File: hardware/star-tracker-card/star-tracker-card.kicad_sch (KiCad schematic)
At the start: 0 parts

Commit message: More EAGLE import cleanup
Fixed sheets, did some ERC cleanup, imported into layout, impmorted 4 layer DRC rules.
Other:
- company: (none) -> Portland State Aerospace Society
- title: (none) -> OreSat Star Tracker

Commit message: Schematic Overhaul of v1.3
Changed schematic to hierarchical, changed debug connector, updated OPD, removed JTAG, and ESD protection on removed connectors
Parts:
- added C42, C43: 22uF, oresat-passives:0805-B-NOSILK, symbol Device:C_Small
- added C45: 10u 25V 0805, Capacitor_SMD:C_1206_3216Metric, symbol Device:C
- added J1: ORESAT-DEBUG-CONNECTOR-CARD, oresat-connectors:J-JST-SM14BSHLSTF, symbol oresat-connectors:ORESAT-DEBUG-CONNECTOR-3
- added J101: 3-1734592-64-1734592-0, star-tracker-card:TE_3-1734592-6, symbol star-tracker-card-eagle-import:3-1734592-64-1734592-0
- added J4: TFM-120-01-L-D-RA, oresat-connectors:J-SAMTEC-TFM-120-X1-XXX-D-RA, symbol oresat-connectors:J-SAMTEC-TFM-120-01-L-D-RA
- added TP183, TP184, TP60, TP61, TP62: TEST-POINT3X4, oresat-misc:TestPoint_Pad_D1.0mm, symbol oresat-misc:Test-Point-1mm-round
- added TP32: Test-Point, oresat-misc:TestPoint_Pad_D1.0mm, symbol oresat-misc:Test-Point-1mm-round
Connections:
- new net: J1.8 (DEBUG-0), TP32.1
- new net: J4.1, J4.2, TP62.1
- new net: J4.5, J4.6, TP60.1
- new net: J4.3, J4.4, TP61.1
- new net: J4.32, J4.33, TP184.1
- new net: J4.34, J4.35, TP183.1
- new net 3.3V: C42.1, C43.1, J101.31, J101.32, J101.33
- new net C3-UART-RX: J4.38
- new net C3-UART-TX: J4.37
- new net CAN2_H: J4.17, J4.18
- new net CAN2_L: J4.19, J4.20
- new net CLK_EN_E: J101.23
- new net D0_E: J101.12
- new net D10_E: J101.16
- new net D11_E: J101.17
- new net D1_E: J101.11
- new net D2_E: J101.10
- new net D3_E: J101.9
- new net D4_E: J101.8
- new net D5_E: J101.7
- new net D6_E: J101.6
- new net D7_E: J101.13
- new net D8_E: J101.14
- new net D9_E: J101.15
- new net FLASH_E: J101.28
- new net GND: C42.2, C43.2, C45.2, J1.14 (GND), J1.15 (PAD), J1.16 (PAD), J1.5 (GND), J101.1, J101.18, J101.19, J101.2, J101.20, J101.34, J101.35, J101.36, J101.S1 (PAD), J101.S2 (PAD), J4.27, J4.28, J4.29, J4.30
- new net HSYNC_E: J101.4
- new net I2C2_SCL: J101.21
- new net I2C2_SDA: J101.22
- new net OPD_PWR: J4.15, J4.16
- new net OPD_SCL: J4.13, J4.14
- new net OPD_SDA: J4.11, J4.12
- new net PIXCLK_E: J101.5
- new net SADDR_E: J101.27
- new net STANDBY_E: J101.25
- new net TRIGGER_E: J101.29
- new net UART0_RX: J1.7 (CARD-RX)
- new net UART0_TX: J1.6 (CARD-TX)
- new net USB_CLI_N: J1.4 (DEVICE-D-)
- new net USB_CLI_P: J1.3 (DEVICE-D+)
- new net VBUS: C45.1, J4.23, J4.24, J4.25, J4.26
- new net VREG_EN_E: J101.30
- new net VSYNC_E: J101.3
- new net V_USB: J1.1 (VBUSP), J1.2 (VBUSP)
- new net ~{OE_E}: J101.26
- new net ~{RESET_E}: J101.24
- no-connect marks 0 -> 15
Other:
- sheet star-tracker-card_2 renamed Card Power Domain
- sheet star-tracker-card_3 renamed SIP C
- sheet star-tracker-card_4 renamed SIP B
- sheet star-tracker-card_5 renamed SIP A, E ,F
- removed sheet star-tracker-card_1
- added sheet Camera Logical Level Shifters (Level_Shifter.kicad_sch)
- added sheet SIP D (SIP_D.kicad_sch)
- sheet Card Power Domain ports: added C3-UART-RX, C3-UART-TX, OPD_PWR, OPD_SCL, OPD_SDA, SW_COM1, SW_COM2; removed none
- sheet SIP A, E ,F ports: added VIN_USB; removed none
- sheet SIP B ports: added USB_CLI_N, USB_CLI_P, USB_CLI_VBUS, VIN_USB; removed none
- sheet SIP C ports: added CAN2_H, CAN2_L, D0_I, D10_I, D11_I, D1_I, D2_I, D3_I, D4_I, D5_I, D6_I, D7_I, D8_I, D9_I, HSYNC_I, PIXCLK_I, SCL_2, SDA_2, UART0_RX, UART0_TX, VSYNCI; removed none
- note added: "36 Pin connector Camera Connector"
- note added: "DOUBLECHECK"
- note added: "Debug Connector"
- note added: "JTAG Connector"
- note added: "Main Connector"
- note added: "Main OreSat Card Connector"
- note added: "Octavo OSD3358-512M-BSM SIP"
- note added: "OreSat Power Domain, creates system wide 5v rail with circuit breaker"

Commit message: Minor update to j4
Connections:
- net at J4.33, TP184.1: now also J4.34; no longer J4.32
- net at J4.35, TP183.1: now also J4.36; no longer J4.34
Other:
- moved on the sheet: TP183
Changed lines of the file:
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@@
 	)
 	(junction
-		(at 49.53 111.76)
-		(diameter 0)
-		(color 0 0 0 0)
-	)
-	(junction
 		(at 359.41 97.79)
 		(diameter 0)
@@
 	)
 	(junction
+		(at 49.53 106.68)
+		(diameter 0)
+		(color 0 0 0 0)
+	)
+	(junction
 		(at 49.53 83.82)
 		(diameter 0.9144)
@@
 	)
 	(junction
-		(at 49.53 106.68)
+		(at 386.08 195.58)
 		(diameter 0)
 		(color 0 0 0 0)
 	)
 	(junction
-		(at 386.08 195.58)
+		(at 49.53 111.76)
 		(diameter 0)
 		(color 0 0 0 0)
@@
 	)
 	(no_connect
+		(at 46.99 104.14)
+	)
+	(no_connect
 		(at 46.99 78.74)
 	)
@@
 	)
 	(no_connect
-		(at 46.99 114.3)
-	)
-	(no_connect
 		(at 46.99 121.92)
 	)
@@
 	(wire
 		(pts
+			(xy 49.53 111.76) (xy 49.53 114.3)
+		)
+		(stroke
+			(width 0)
+			(type default)
+		)
+	)
+	(wire
+		(pts
 			(xy 386.08 104.14) (xy 391.16 104.14)
 		)
@@
 	(wire
 		(pts
+			(xy 49.53 106.68) (xy 69.85 106.68)
+		)
+		(stroke
+			(width 0)
+			(type default)
+		)
+	)
+	(wire
+		(pts
 			(xy 171.45 119.38) (xy 190.5 119.38)
 		)
@@
 	(wire
 		(pts
-			(xy 46.99 106.68) (xy 49.53 106.68)
-		)
-		(stroke
-			(width 0)
-			(type default)
-		)
-	)
-	(wire
-		(pts
 			(xy 48.26 50.8) (xy 48.26 53.34)
 		)
@@
 	(wire
 		(pts
-			(xy 49.53 104.14) (xy 49.53 106.68)
-		)
-		(stroke
-			(width 0)
-			(type default)
-		)
-	)
-	(wire
-		(pts
 			(xy 48.26 25.4) (xy 69.85 25.4)
 		)
@@
 	(wire
 		(pts
-			(xy 49.53 109.22) (xy 49.53 111.76)
-		)
-		(stroke
-			(width 0)
-			(type default)
-		)
-	)
-	(wire
-		(pts
 			(xy 48.26 66.04) (xy 48.26 68.58)
 		)
@@
 	(wire
 		(pts
+			(xy 49.53 109.22) (xy 49.53 106.68)
+		)
+		(stroke
+			(width 0)
+			(type default)
+		)
+	)
+	(wire
+		(pts
 			(xy 168.91 116.84) (xy 190.5 116.84)
 		)
@@
 	(wire
 		(pts
+			(xy 46.99 109.22) (xy 49.53 109.22)
+		)
+		(stroke
+			(width 0)
+			(type default)
+		)
+	)
+	(wire
+		(pts
 			(xy 386.08 111.76) (xy 386.08 109.22)
 		)
@@
 	(wire
 		(pts
-			(xy 49.53 106.68) (xy 69.85 106.68)
+			(xy 46.99 106.68) (xy 49.53 106.68)
 		)
 		(stroke
@@
 	(wire
 		(pts
-			(xy 49.53 111.76) (xy 69.85 111.76)
-		)
-		(stroke
-			(width 0)
-			(type default)
-		)
-	)
-	(wire
-		(pts
 			(xy 236.22 184.15) (xy 265.43 184.15)
 		)
@@
 	(wire
 		(pts
-			(xy 46.99 104.14) (xy 49.53 104.14)
+			(xy 308.61 167.64) (xy 391.16 167.64)
 		)
 		(stroke
@@
 	(wire
 		(pts
-			(xy 308.61 167.64) (xy 391.16 167.64)
+			(xy 308.61 139.7) (xy 391.16 139.7)
 		)
 		(stroke
@@
 	(wire
 		(pts
-			(xy 308.61 139.7) (xy 391.16 139.7)
+			(xy 378.46 147.32) (xy 378.46 148.59)
 		)
 		(stroke
-			(width 0)
-			(type default)
+			(width 0.1524)
+			(type solid)
 		)
 	)
 	(wire
 		(pts
-			(xy 378.46 147.32) (xy 378.46 148.59)
+			(xy 49.53 111.76) (xy 69.85 111.76)
 		)
 		(stroke
-			(width 0.1524)
-			(type solid)
+			(width 0)
+			(type default)
 		)
 	)
@@
 	(wire
 		(pts
-			(xy 46.99 25.4) (xy 48.26 25.4)
+			(xy 46.99 114.3) (xy 49.53 114.3)
 		)
 		(stroke
@@
 	(wire
 		(pts
-			(xy 46.99 27.94) (xy 48.26 27.94)
+			(xy 46.99 25.4) (xy 48.26 25.4)
 		)
 		(stroke
@@
 	(wire
 		(pts
-			(xy 234.95 115.57) (xy 265.43 115.57)
+			(xy 46.99 27.94) (xy 48.26 27.94)
 		)
 		(stroke
@@
 	(wire
 		(pts
-			(xy 391.16 106.68) (xy 386.08 106.68)
+			(xy 234.95 115.57) (xy 265.43 115.57)
 		)
 		(stroke
-			(width 0.1524)
-			(type solid)
+			(width 0)
+			(type default)
 		)
 	)
 	(wire
 		(pts
-			(xy 46.99 109.22) (xy 49.53 109.22)
+			(xy 391.16 106.68) (xy 386.08 106.68)
 		)
 		(stroke
-			(width 0)
-			(type default)
+			(width 0.1524)
+			(type solid)
 		)
 	)
@@
 	(wire
 		(pts
-			(xy 69.85 111.76) (xy 69.85 113.03)
-		)
-		(stroke
-			(width 0)
-			(type default)
-		)
-	)
-	(wire
-		(pts
 			(xy 234.95 127) (xy 265.43 127)
 		)
@@
 	(symbol
 		(lib_id "oresat-misc:Test-Point-1mm-round")
-		(at 69.85 113.03 0)
+		(at 69.85 111.76 0)
 		(unit 1)
 		(exclude_from_sim yes)
@@
 		(dnp no)
 		(property "Reference" "TP183"
-			(at 74.422 113.792 0)
+			(at 74.422 112.522 0)
 			(effects
 				(font
@@
 		)
 		(property "Value" "TEST-POINT3X4"
-			(at 67.31 115.57 0)
+			(at 67.31 114.3 0)
 			(effects
 				(font
@@
 		)
 		(property "Footprint" "oresat-misc:TestPoint_Pad_D1.0mm"
-			(at 69.85 102.87 0)
+			(at 69.85 101.6 0)
 			(effects
 				(font
@@
 		)
 		(property "Datasheet" ""
-			(at 69.85 113.03 0)
+			(at 69.85 111.76 0)
 			(effects
 				(font
@@
 		)
 		(property "Description" "1mm round SMT test point"
-			(at 69.85 113.03 0)
+			(at 69.85 111.76 0)
 			(effects
 				(font

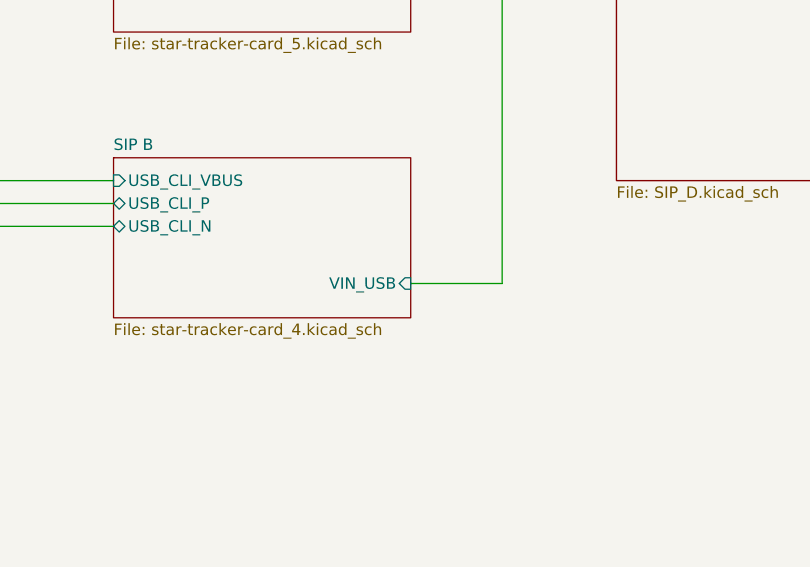
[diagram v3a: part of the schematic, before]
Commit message: Updated Octavo schematic
Removed many testpoints, added filter to 1.8v reference, tied some signals to ground with pull down resistor, added NCs to multiple pins.
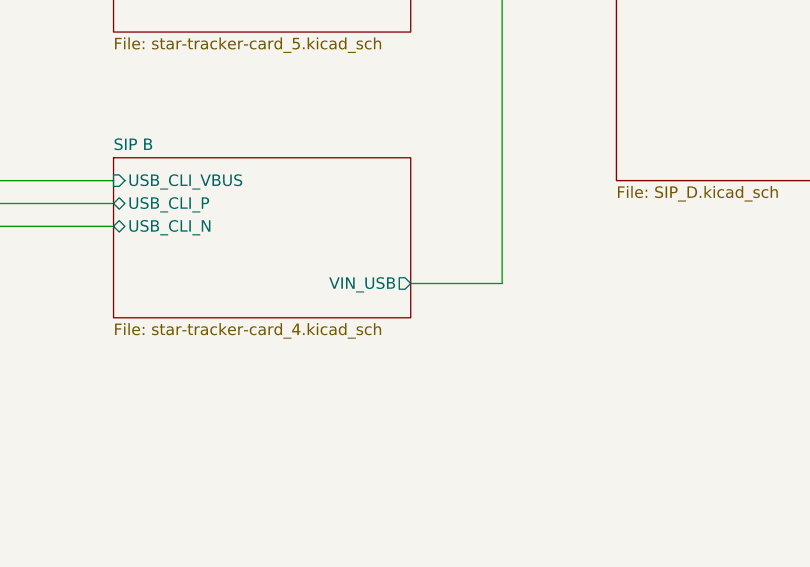
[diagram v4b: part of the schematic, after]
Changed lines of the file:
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@@
-			)
-		)
-		(pin "VIN_USB" input
-			(at 167.64 214.63 0)
-			(effects
-				(font
-					(size 1.27 1.27)
-				)
-				(justify right)
 			)
 		)
@@
 			)
 		)
+		(pin "VIN_USB" output
+			(at 167.64 214.63 0)
+			(effects
+				(font
+					(size 1.27 1.27)
+				)
+				(justify right)
+			)
+		)

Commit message: Update
Update to the octavo schematic
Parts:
- removed TP60, TP61, TP62: TEST-POINT3X4, oresat-misc:TestPoint_Pad_D1.0mm, symbol oresat-misc:Test-Point-1mm-round
- added J7: GRPB041VWVN-RC, Connector_PinHeader_1.27mm:PinHeader_1x04_P1.27mm_Vertical, symbol Connector_Generic:Conn_01x04
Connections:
- net GND: now also J7.4 (Pin_4)
- net at J4.1: no longer J4.2
- net at J4.5: no longer J4.6
- net at J4.3: no longer J4.4
- new net SIP A/EEPROM_WP: J7.3 (Pin_3)
- new net SIP A/PMIC_SCL: J7.1 (Pin_1)
- new net SIP A/PMIC_SDA: J7.2 (Pin_2)
- no-connect marks 15 -> 21
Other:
- sheet SIP A, E ,F renamed SIP A
- added sheet SIP E+F (SIP_E.kicad_sch)
- sheet SIP A ports: added EEPROM_WP, PMIC_SCL, PMIC_SDA, nRESET; removed none
- sheet SIP B ports: added nRESET; removed VIN_USB
- note added: "Porgram Boot EEPROM"
- note removed: "JTAG Connector"

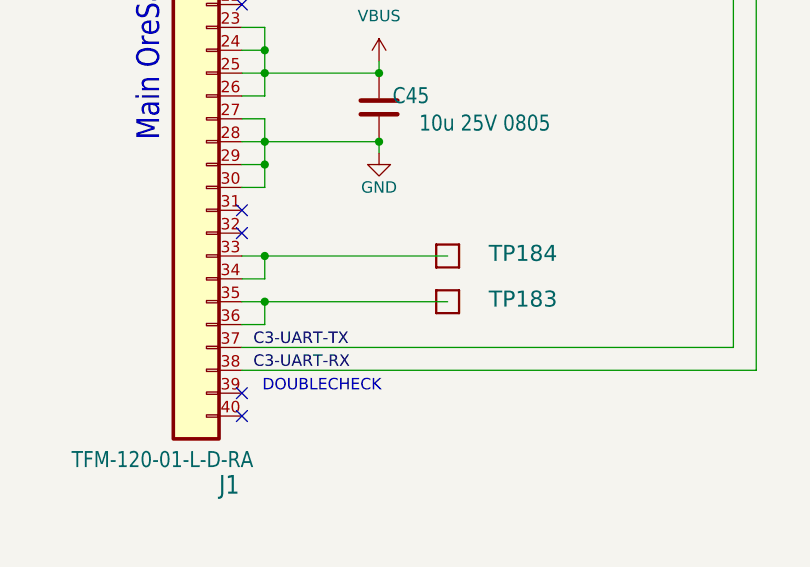
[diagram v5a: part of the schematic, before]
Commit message: Small Update
Removed couple more test points added 2 100nF caps and added text to out put possible pins connected to pull down resistors.
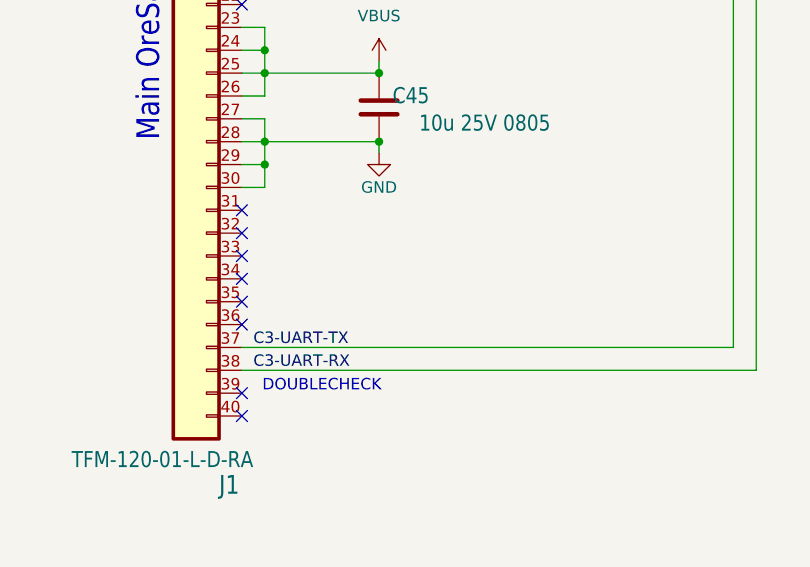
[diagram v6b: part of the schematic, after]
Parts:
- removed TP183, TP184: TEST-POINT3X4, oresat-misc:TestPoint_Pad_D1.0mm, symbol oresat-misc:Test-Point-1mm-round
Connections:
- net at J4.33: no longer J4.34
- net at J4.35: no longer J4.36
- no-connect marks 21 -> 25
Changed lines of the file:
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@@
 	)
 	(junction
-		(at 49.53 106.68)
-		(diameter 0)
-		(color 0 0 0 0)
-	)
-	(junction
 		(at 49.53 83.82)
 		(diameter 0.9144)
@@
 	)
 	(junction
-		(at 49.53 111.76)
-		(diameter 0)
-		(color 0 0 0 0)
-	)
-	(junction
 		(at 49.53 86.36)
 		(diameter 0.9144)
@@
 	)
 	(no_connect
+		(at 46.99 106.68)
+	)
+	(no_connect
 		(at 46.99 43.18)
 	)
@@
 	)
 	(no_connect
+		(at 46.99 114.3)
+	)
+	(no_connect
+		(at 46.99 111.76)
+	)
+	(no_connect
 		(at 46.99 48.26)
 	)
@@
 	)
 	(no_connect
+		(at 46.99 109.22)
+	)
+	(no_connect
 		(at 57.15 163.83)
 	)
@@
 	(wire
 		(pts
-			(xy 49.53 111.76) (xy 49.53 114.3)
-		)
-		(stroke
-			(width 0)
-			(type default)
-		)
-	)
-	(wire
-		(pts
 			(xy 386.08 104.14) (xy 391.16 104.14)
 		)
@@
 	(wire
 		(pts
-			(xy 49.53 106.68) (xy 69.85 106.68)
-		)
-		(stroke
-			(width 0)
-			(type default)
-		)
-	)
-	(wire
-		(pts
 			(xy 171.45 119.38) (xy 190.5 119.38)
 		)
@@
 	(wire
 		(pts
-			(xy 49.53 109.22) (xy 49.53 106.68)
-		)
-		(stroke
-			(width 0)
-			(type default)
-		)
-	)
-	(wire
-		(pts
 			(xy 168.91 116.84) (xy 190.5 116.84)
 		)
@@
 	(wire
 		(pts
-			(xy 46.99 109.22) (xy 49.53 109.22)
-		)
-		(stroke
-			(width 0)
-			(type default)
-		)
-	)
-	(wire
-		(pts
 			(xy 386.08 111.76) (xy 386.08 109.22)
 		)
@@
 	(wire
 		(pts
-			(xy 46.99 111.76) (xy 49.53 111.76)
-		)
-		(stroke
-			(width 0)
-			(type default)
-		)
-	)
-	(wire
-		(pts
 			(xy 134.62 204.47) (xy 87.63 204.47)
 		)
@@
 	(wire
 		(pts
-			(xy 46.99 106.68) (xy 49.53 106.68)
-		)
-		(stroke
-			(width 0)
-			(type default)
-		)
-	)
-	(wire
-		(pts
 			(xy 234.95 144.78) (xy 265.43 144.78)
 		)
@@
 	(wire
 		(pts
-			(xy 49.53 111.76) (xy 69.85 111.76)
-		)
-		(stroke
-			(width 0)
-			(type default)
-		)
-	)
-	(wire
-		(pts
 			(xy 308.61 175.26) (xy 391.16 175.26)
 		)
@@
 	(wire
 		(pts
-			(xy 46.99 114.3) (xy 49.53 114.3)
-		)
-		(stroke
-			(width 0)
-			(type default)
-		)
-	)
-	(wire
-		(pts
 			(xy 92.71 224.79) (xy 134.62 224.79)
 		)
@@
 	)
 	(symbol
-		(lib_id "oresat-misc:Test-Point-1mm-round")
-		(at 69.85 106.68 0)
-		(unit 1)
-		(exclude_from_sim yes)
-		(in_bom no)
-		(on_board yes)
-		(dnp no)
-		(property "Reference" "TP184"
-			(at 74.422 107.442 0)
-			(effects
-				(font
-					(size 1.778 1.778)
-				)
-				(justify left bottom)
-			)
-		)
-		(property "Value" "TEST-POINT3X4"
-			(at 67.31 109.22 0)
-			(effects
-				(font
-					(size 1.778 1.778)
-				)
-				(justify left bottom)
-				(hide yes)
-			)
-		)
-		(property "Footprint" "oresat-misc:TestPoint_Pad_D1.0mm"
-			(at 69.85 96.52 0)
-			(effects
-				(font
-					(size 1.27 1.27)
-				)
-				(hide yes)
-			)
-		)
-		(property "Datasheet" ""
-			(at 69.85 106.68 0)
-			(effects
-				(font
-					(size 1.27 1.27)
-				)
-				(hide yes)
-			)
-		)
-		(property "Description" "1mm round SMT test point"
-			(at 69.85 106.68 0)
-			(effects
-				(font
-					(size 1.27 1.27)
-				)
-				(hide yes)
-			)
-		)
-		(pin "1"
-		)
-		(instances
-			(project "star-tracker-card"
-				(path "/324e9eb5-7420-4b7e-862c-cc20bb28618a"
-					(reference "TP184")
-					(unit 1)
-				)
-			)
-		)
-	)
-	(symbol
 		(lib_id "power:GND")
 		(at 46.99 193.04 0)
@@
 					(unit 1)
 				)
-			)
-		)
-	)
-	(symbol
-		(lib_id "oresat-misc:Test-Point-1mm-round")
-		(at 69.85 111.76 0)
-		(unit 1)
-		(exclude_from_sim yes)
-		(in_bom no)
-		(on_board yes)
-		(dnp no)
-		(property "Reference" "TP183"
-			(at 74.422 112.522 0)
-			(effects
-				(font
-					(size 1.778 1.778)
-				)
-				(justify left bottom)
-			)
-		)
-		(property "Value" "TEST-POINT3X4"
-			(at 67.31 114.3 0)
-			(effects
-				(font
-					(size 1.778 1.778)
-				)
-				(justify left bottom)
-				(hide yes)
-			)
-		)
-		(property "Footprint" "oresat-misc:TestPoint_Pad_D1.0mm"
-			(at 69.85 101.6 0)
-			(effects
-				(font
-					(size 1.27 1.27)
-				)
-				(hide yes)
-			)
-		)
-		(property "Datasheet" ""
-			(at 69.85 111.76 0)
-			(effects
-				(font
-					(size 1.27 1.27)
-				)
-				(hide yes)
-			)
-		)
-		(property "Description" "1mm round SMT test point"
-			(at 69.85 111.76 0)
-			(effects
-				(font
-					(size 1.27 1.27)
-				)
-				(hide yes)
-			)
-		)
-		(pin "1"
-		)
-		(instances
-			(project "star-tracker-card"
-				(path "/324e9eb5-7420-4b7e-862c-cc20bb28618a"
-					(reference "TP183")
-					(unit 1)
-				)

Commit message: Big almost-done cleanup
Fixed a bunch of things in the schematic. Compared against C3 Octavo. Fixed all weird ERCs. Cleaned up a lot of planes on the layout. Moved uart switch, rerouted a bunch of traces for better layout. Fixed library issues, and board/sch sync issues.
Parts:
- C42, C43: value 22uF -> 22u; footprint oresat-passives:0805-B-NOSILK -> Capacitor_SMD:C_1210_3225Metric
- C45: value 10u 25V 0805 -> 10u; footprint Capacitor_SMD:C_1206_3216Metric -> oresat-passives:0805-B-NOSILK; DIS DigiKey -> (none); DPN 587-3485-1-ND -> (none); MFR Taiyo Yuden -> (none); MPN TMK316AB7106KLHT -> (none)
- J1: value ORESAT-DEBUG-CONNECTOR-CARD -> SM14B-SHLS-TF
- J7: DST DigiKey -> (none)
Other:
- sheet Card Power Domain ports: added UART0_RX, UART0_TX; removed SW_COM1, SW_COM2
- note added: "0805"
- note added: "Needed for programming boot EEPROM TPS65217 I2C Addrs = 0x24 EEPROM I2C Addrs = 0x50 Needs 4 pos 1.27 mm socket and cable, e.g., Samtec SFSS-04-28-H-06.00-SR."
- note removed: "DOUBLECHECK"
- note removed: "Debug Connector"
- note removed: "OreSat Power Domain, creates system wide 5v rail with circuit breaker"
- note removed: "Porgram Boot EEPROM"
- moved on the sheet: J7, TP32

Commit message: BOM 99% completed, push for final review
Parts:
- C42, C43: footprint Capacitor_SMD:C_1210_3225Metric -> Capacitor_SMD:C_0805_2012Metric; DIS (none) -> DigiKey; DPN (none) -> 478-KAM21AT70J226KUCT-ND; MFR (none) -> KYOCERA AVX; MPN (none) -> KAM21AT70J226KU
- C45: DIS (none) -> DigiKey; DPN (none) -> 490-GRT21BC71E106KE13KCT-ND; MFR (none) -> Murata Electronics; MPN (none) -> GRT21BC71E106KE13K
- J101: DIS (none) -> DigiKey; DPN (none) -> A100290CT-ND; MFR (none) -> TE Connectivity AMP Connectors; MPN (none) -> 3-1734592-0
- J4: DIS (none) -> DigiKey; DPN (none) -> SAM10145-ND; MFR (none) -> Samtec Inc.; MPN (none) -> TFM-120-01-L-D-RA
